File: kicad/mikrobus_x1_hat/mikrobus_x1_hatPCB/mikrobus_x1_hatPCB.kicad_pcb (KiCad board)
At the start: 2 copper layers, 65 x 56.5 mm, 6 parts, among them IC1 MIKROE-924, J1 RPi_GPIO

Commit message: schematic complete with 0 ERC errors
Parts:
- moved IC1 22.3 mm to (159.2, 107.7), turned to 180 degrees
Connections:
- IC1 pad 1: unconnected-(IC1-AN-Pad1) -> Net-(IC1-AN)
- IC1 pad 10: unconnected-(IC1-INT-Pad10) -> Net-(IC1-INT)
- IC1 pad 11: unconnected-(IC1-RX-Pad11) -> Net-(IC1-RX)
- IC1 pad 12: unconnected-(IC1-TX-Pad12) -> Net-(IC1-TX)
- IC1 pad 13: unconnected-(IC1-SCL-Pad13) -> Net-(IC1-SCL)
- IC1 pad 14: unconnected-(IC1-SDA-Pad14) -> Net-(IC1-SDA)
- IC1 pad 15: unconnected-(IC1-+5V-Pad15) -> 5V
- IC1 pad 16: unconnected-(IC1-GND_2-Pad16) -> GND
- IC1 pad 2: unconnected-(IC1-RST-Pad2) -> Net-(IC1-RST)
- IC1 pad 3: unconnected-(IC1-CS-Pad3) -> Net-(IC1-CS)
- IC1 pad 4: unconnected-(IC1-SCK-Pad4) -> Net-(IC1-SCK)
- IC1 pad 5: unconnected-(IC1-MISO-Pad5) -> Net-(IC1-MISO)
- IC1 pad 6: unconnected-(IC1-MOSI-Pad6) -> Net-(IC1-MOSI)
- IC1 pad 7: unconnected-(IC1-+3.3V-Pad7) -> 3V3
- IC1 pad 8: unconnected-(IC1-GND_1-Pad8) -> GND
- IC1 pad 9: unconnected-(IC1-PWM-Pad9) -> Net-(IC1-PWM)
- J1 pad 1: unconnected-(J1-3.3V-Pad1) -> 3V3
- J1 pad 10: unconnected-(J1-BCM15_RXD-Pad10) -> Net-(IC1-RX)
- J1 pad 11: unconnected-(J1-BCM17-Pad11) -> Net-(IC1-INT)
- J1 pad 12: unconnected-(J1-BCM18_PCM_C-Pad12) -> Net-(IC1-PWM)
- J1 pad 14: unconnected-(J1-GND-Pad14) -> GND
- J1 pad 15: unconnected-(J1-BCM22-Pad15) -> Net-(IC1-AN)
- J1 pad 17: unconnected-(J1-3.3V-Pad17) -> 3V3
- J1 pad 19: unconnected-(J1-BCM10_MOSI-Pad19) -> Net-(IC1-MOSI)
- J1 pad 2: unconnected-(J1-5V-Pad2) -> 5V
- J1 pad 20: unconnected-(J1-GND-Pad20) -> GND
- J1 pad 21: unconnected-(J1-BCM9_MISO-Pad21) -> Net-(IC1-MISO)
- J1 pad 23: unconnected-(J1-BCM11_SCLK-Pad23) -> Net-(IC1-SCK)
- J1 pad 24: unconnected-(J1-BCM8_CE0-Pad24) -> Net-(IC1-CS)
- J1 pad 25: unconnected-(J1-GND-Pad25) -> GND
- J1 pad 3: unconnected-(J1-BCM2_SDA-Pad3) -> Net-(IC1-SDA)
- J1 pad 30: unconnected-(J1-GND-Pad30) -> GND
- J1 pad 34: unconnected-(J1-GND-Pad34) -> GND
- J1 pad 39: unconnected-(J1-GND-Pad39) -> GND
- J1 pad 4: unconnected-(J1-5V-Pad4) -> 5V
- J1 pad 5: unconnected-(J1-BCM3_SCL-Pad5) -> Net-(IC1-SCL)
- J1 pad 6: unconnected-(J1-GND-Pad6) -> GND
- J1 pad 7: unconnected-(J1-BCM4_GPCLK0-Pad7) -> Net-(IC1-RST)
- J1 pad 8: unconnected-(J1-BCM14_TXD-Pad8) -> Net-(IC1-TX)
- J1 pad 9: unconnected-(J1-GND-Pad9) -> GND
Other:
- board text removed: "Dimensions taken from https://github.com/raspberrypi/hats/blob/master/hat-board-mechanical.pdf"
- board text removed: "Select one of these board edges depending upon the type of socket that is used."

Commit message: pcb routing initiated
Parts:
- moved IC1 3.27 mm to (160.0, 104.5)
- moved J1 0.81 mm to (147.9, 75.3)
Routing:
- net GND: track 0.00 -> 44.9 mm, vias 0 -> 4
- net 3V3: track 0.00 -> 42.7 mm, vias 0 -> 2
- net Net-(IC1-RST): track 0.00 -> 39.2 mm, vias 0 -> 2
- net Net-(IC1-CS): track 0.00 -> 36.4 mm
- net Net-(IC1-PWM): track 0.00 -> 35.7 mm
- net Net-(IC1-AN): track 0.00 -> 34.1 mm
- net Net-(IC1-RX): track 0.00 -> 30.4 mm
- net Net-(IC1-TX): track 0.00 -> 29.9 mm
- net Net-(IC1-SCK): track 0.00 -> 27.8 mm
- net Net-(IC1-INT): track 0.00 -> 27.2 mm
- net Net-(IC1-MISO): track 0.00 -> 26.1 mm
- net Net-(IC1-MOSI): track 0.00 -> 25.9 mm
- net 5V: track 0.00 -> 23.7 mm
- net Net-(IC1-SCL): track 0.00 -> 22.5 mm
- net Net-(IC1-SDA): track 0.00 -> 18.2 mm
- added copper zone on F.Cu, net GND
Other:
- outline, holes or cut-outs redrawn

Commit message: PCB completed
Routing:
- net GND: track 44.9 -> 17.8 mm, vias 4 -> 2
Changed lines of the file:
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@@
 			)
 		)
-		(property "Footprint" "MIKROE924"
+		(property "Footprint" "MIKROE-924:MIKROE924"
 			(at 0 0 180)
 			(unlocked yes)
@@
 	)
 	(segment
-		(start 138.4 87.98)
-		(end 138.4 91.9925)
-		(width 0.25)
-		(layer "F.Cu")
-		(net 11)
-	)
-	(segment
-		(start 159.98 86.7)
-		(end 160.506942 86.7)
-		(width 0.25)
-		(layer "F.Cu")
-		(net 11)
-	)
-	(segment
-		(start 161.0275 87.7475)
-		(end 161.0275 89.673889)
-		(width 0.25)
-		(layer "F.Cu")
-		(net 11)
-	)
-	(segment
-		(start 133.89 78.0356)
-		(end 132.88 77.0256)
-		(width 0.25)
-		(layer "F.Cu")
-		(net 11)
-	)
-	(segment
-		(start 137.12 93.2725)
-		(end 135.2775 93.2725)
-		(width 0.25)
-		(layer "F.Cu")
-		(net 11)
-	)
-	(segment
-		(start 159.981389 90.72)
-		(end 158.87 90.72)
-		(width 0.25)
-		(layer "F.Cu")
-		(net 11)
-	)
-	(segment
-		(start 137.12 86.7)
-		(end 138.4 87.98)
-		(width 0.25)
-		(layer "F.Cu")
-		(net 11)
-	)
-	(segment
 		(start 132.01 82.54)
 		(end 132.01 82.6)
@@
 	)
 	(segment
-		(start 132.88 77.0256)
-		(end 132.88 72.37)
-		(width 0.25)
-		(layer "F.Cu")
-		(net 11)
-	)
-	(segment
 		(start 137.12 86.7)
 		(end 136.17 86.7)
@@
 	)
 	(segment
-		(start 132.88 72.37)
-		(end 132.55 72.04)
-		(width 0.25)
-		(layer "F.Cu")
-		(net 11)
-	)
-	(segment
-		(start 159.98 86.7)
-		(end 161.0275 87.7475)
-		(width 0.25)
-		(layer "F.Cu")
-		(net 11)
-	)
-	(segment
-		(start 138.4 91.9925)
-		(end 137.12 93.2725)
-		(width 0.25)
-		(layer "F.Cu")
-		(net 11)
-	)
-	(segment
 		(start 133.89 79.68)
 		(end 135.09 80.88)
@@
 	)
 	(segment
-		(start 160.506942 86.7)
-		(end 161.225 85.981942)
-		(width 0.25)
-		(layer "F.Cu")
-		(net 11)
-	)
-	(segment
 		(start 133.89 78.0356)
 		(end 133.89 79.68)
@@
 	)
 	(segment
-		(start 135.2775 93.2725)
-		(end 135.24 93.31)
-		(width 0.25)
-		(layer "F.Cu")
-		(net 11)
-	)
-	(segment
-		(start 161.0275 89.673889)
-		(end 159.981389 90.72)
-		(width 0.25)
-		(layer "F.Cu")
-		(net 11)
-	)
-	(segment
 		(start 136.17 86.7)
 		(end 132.01 82.54)
@@
 	(via
 		(at 130.56 81.09)
-		(size 0.6)
-		(drill 0.4)
-		(layers "F.Cu" "B.Cu")
-		(net 11)
-	)
-	(via
-		(at 161.225 85.981942)
 		(size 0.6)
 		(drill 0.4)
@@
 		(net 11)
 	)
-	(via
-		(at 164.75 86.02)
-		(size 0.6)
-		(drill 0.4)
-		(layers "F.Cu" "B.Cu")
-		(net 11)
-	)
-	(segment
-		(start 164.711942 85.981942)
-		(end 164.75 86.02)
+	(segment
+		(start 135.09 80.88)
+		(end 134.055 79.845)
 		(width 0.25)
 		(layer "B.Cu")
@@
 	)
 	(segment
-		(start 161.225 85.981942)
-		(end 164.711942 85.981942)
+		(start 134.055 79.845)
+		(end 131.805 79.845)
 		(width 0.25)
 		(layer "B.Cu")
@@
 	)
 	(segment
-		(start 135.09 80.88)
-		(end 134.055 79.845)
+		(start 131.805 79.845)
+		(end 130.56 81.09)
 		(width 0.25)
 		(layer "B.Cu")
@@
 	)
 	(segment
-		(start 134.055 79.845)
-		(end 131.805 79.845)
-		(width 0.25)
-		(layer "B.Cu")
-		(net 11)
-	)
-	(segment
-		(start 131.805 79.845)
-		(end 130.56 81.09)
-		(width 0.25)
-		(layer "B.Cu")
-		(net 11)
+		(start 137.12 94.32)
+		(end 139 92.44)
+		(width 0.25)
+		(layer "F.Cu")
+		(net 12)
 	)
 	(segment
 		(start 139 92.44)
-		(end 139 86.1)
+		(end 139 85.75)
 		(width 0.25)
 		(layer "F.Cu")
@@
 	)
 	(segment
-		(start 139 86.1)
-		(end 137.75 84.85)
+		(start 138.1 84.85)
+		(end 135.6244 84.85)
+		(width 0.25)
+		(layer "F.Cu")
+		(net 12)
+	)
+	(segment
+		(start 139 85.75)
+		(end 138.1 84.85)
 		(width 0.25)
 		(layer "F.Cu")
@@
 		(start 135.6244 84.85)
 		(end 128.81 78.0356)
-		(width 0.25)
-		(layer "F.Cu")
-		(net 12)
-	)
-	(segment
-		(start 137.75 84.85)
-		(end 135.6244 84.85)
-		(width 0.25)
-		(layer "F.Cu")
-		(net 12)
-	)
-	(segment
-		(start 137.12 94.32)
-		(end 139 92.44)
 		(width 0.25)
 		(layer "F.Cu")
@@
 		(hatch edge 0.5)
 		(connect_pads
-			(clearance 0.508)
+			(clearance 0.18)
 		)
 		(min_thickness 0.25)
@@
 		(polygon
 			(pts
-				(xy 172.61 126.39) (xy 123.61 126.52) (xy 123.65 119) (xy 117.49 119.16) (xy 117.49 109.91) (xy 121.75 109.55)
-				(xy 122.12 88.85) (xy 117.25 88.72) (xy 117.25 79.96) (xy 122.29 79.93) (xy 122.3 70.84) (xy 173.08 70.86)
-				(xy 173.29 79.45) (xy 179.14 79.35) (xy 178.77 117.8) (xy 172.44 117.71) (xy 172.59 125.05) (xy 172.59 125.93)
-			)
-		)
+				(xy 117.93 70.68) (xy 177.42 70.65) (xy 178.59 71.04) (xy 179 71.31) (xy 179.46 71.76) (xy 179.87 72.5)
+				(xy 180.04 73.45) (xy 180.03 124.14) (xy 179.72 125.31) (xy 178.87 126.35) (xy 177.56 126.9) (xy 175.54 126.86)
+				(xy 119.22 126.9) (xy 117.66 126.87) (xy 116.75 126.52) (xy 116.08 125.96) (xy 115.4 124.9) (xy 115.28 123.94)
+				(xy 115.36 108.24) (xy 115.92 107.69) (xy 119.21 107.67) (xy 119.91 107.42) (xy 120.3 106.76) (xy 120.3 104.19)
+				(xy 120.32 98.32) (xy 120.26 91.24) (xy 119.95 90.73) (xy 119.44 90.4) (xy 116.15 90.39) (xy 115.72 90.23)
+				(xy 115.3 89.75) (xy 115.3 88.37) (xy 115.32 72.94) (xy 116.02 71.64) (xy 116.86 70.97) (xy 117.68 70.69)
+			)
+		)

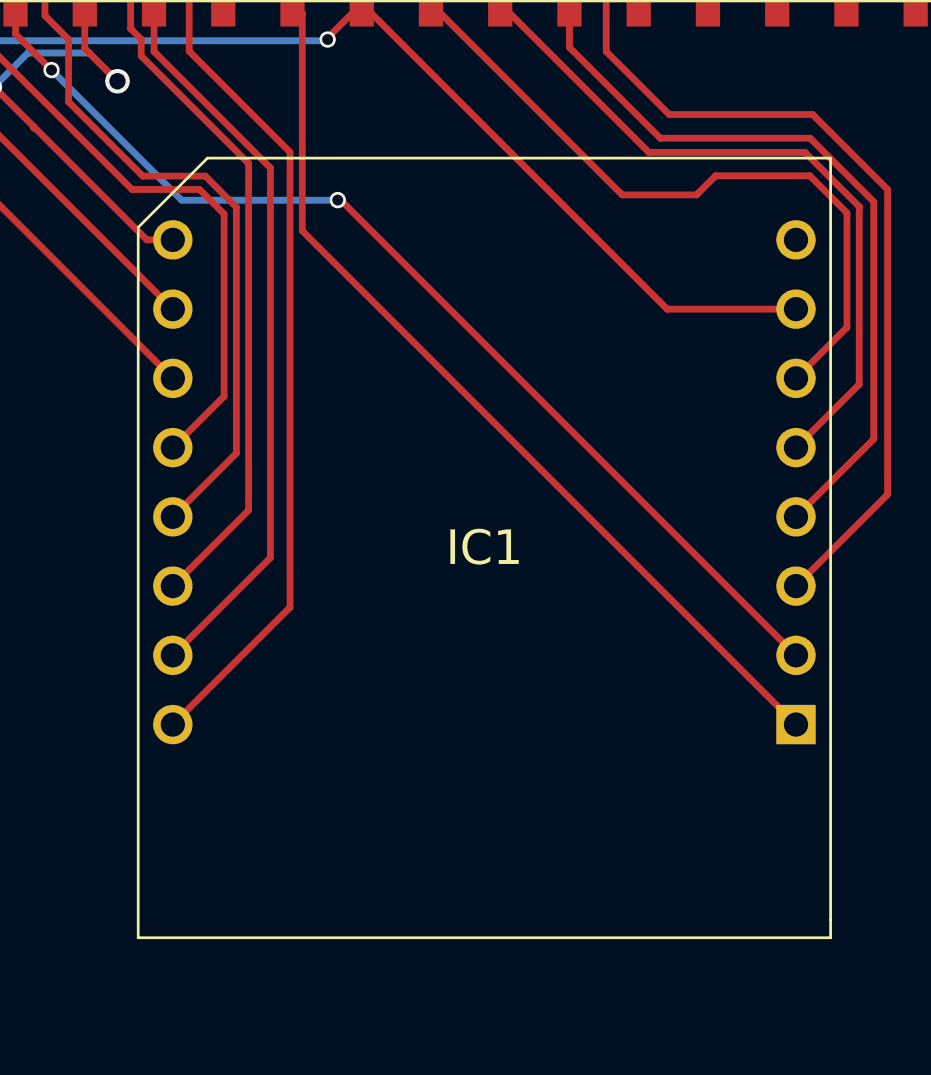
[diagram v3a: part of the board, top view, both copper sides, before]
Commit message: MikroBUS logo added
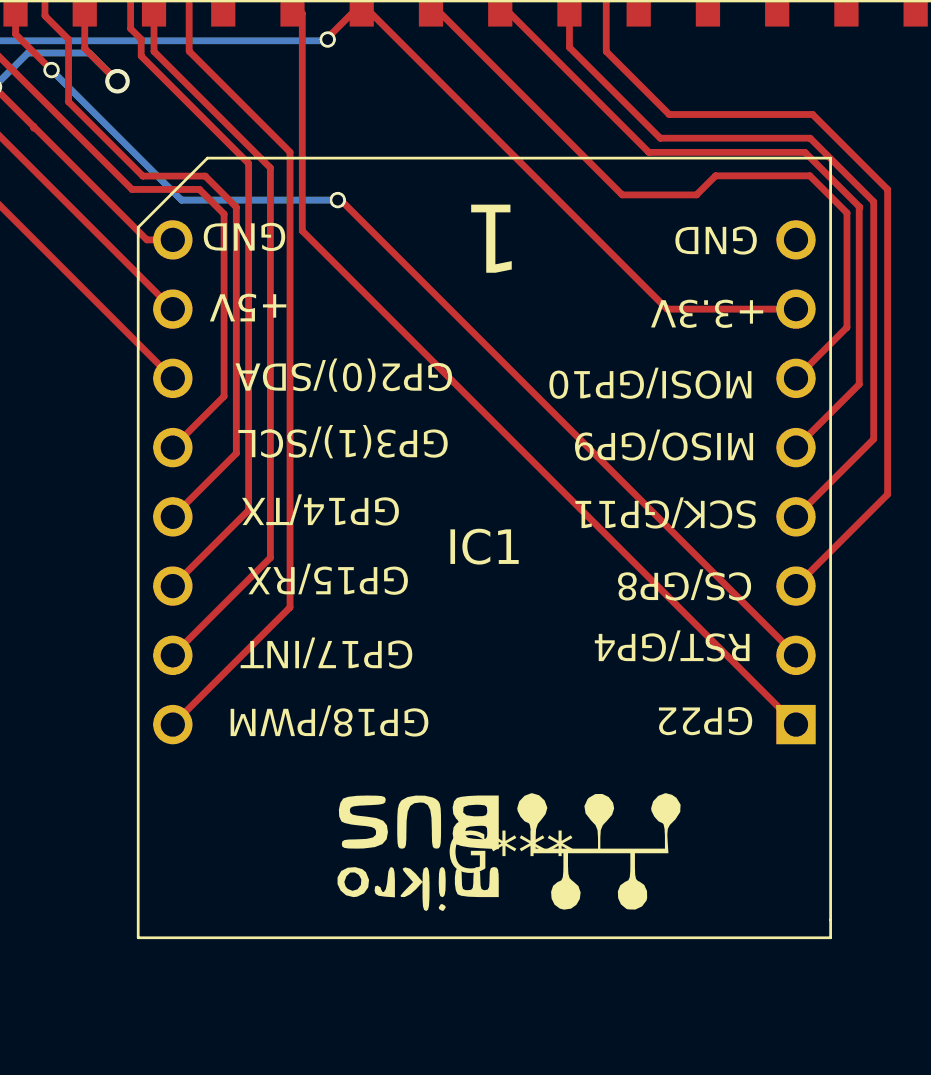
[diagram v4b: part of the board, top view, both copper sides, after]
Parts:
- added G***: LOGO, logo:mikro_logo, F.Cu at (149.5, 109.2)
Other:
- board text added: "+3.3V"
- board text added: "+5V"
- board text added: "1"
- board text added: "CS/GP8"
- board text added: "GND"
- board text added: "GP14/TX"
- board text added: "GP15/RX"
- board text added: "GP17/INT"
- board text added: "GP18/PWM"
- board text added: "GP2(0)/SDA"
- board text added: "GP22"
- board text added: "GP3(1)/SCL"
- board text added: "MISO/GP9"
- board text added: "MOSI/GP10"
- board text added: "RST/GP4"
- board text added: "SCK/GP11"
